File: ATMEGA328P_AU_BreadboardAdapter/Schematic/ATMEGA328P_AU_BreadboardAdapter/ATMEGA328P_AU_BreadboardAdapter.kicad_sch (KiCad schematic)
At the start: 23 parts, among them J1 FTDI, J2 Pin header 1, J3 Pin header 2, SW1 RESET, U1 AMS1117-5.0, U2 ATMEGA328P-AU, Y1 16MHz

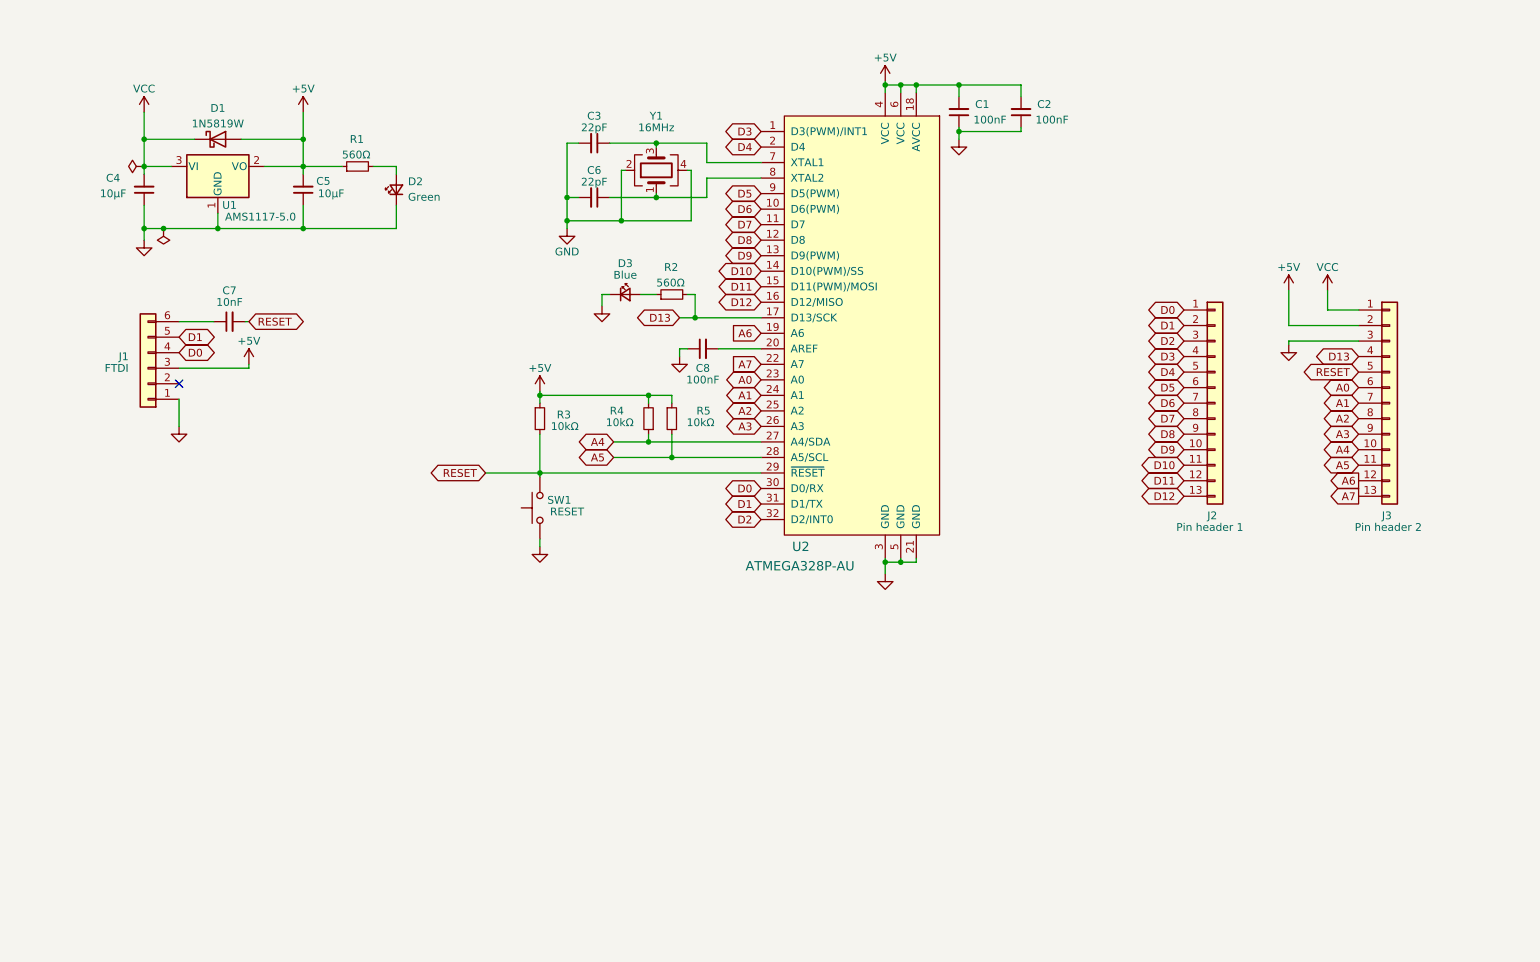
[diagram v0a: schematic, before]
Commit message: LDO replaced by buck regulator
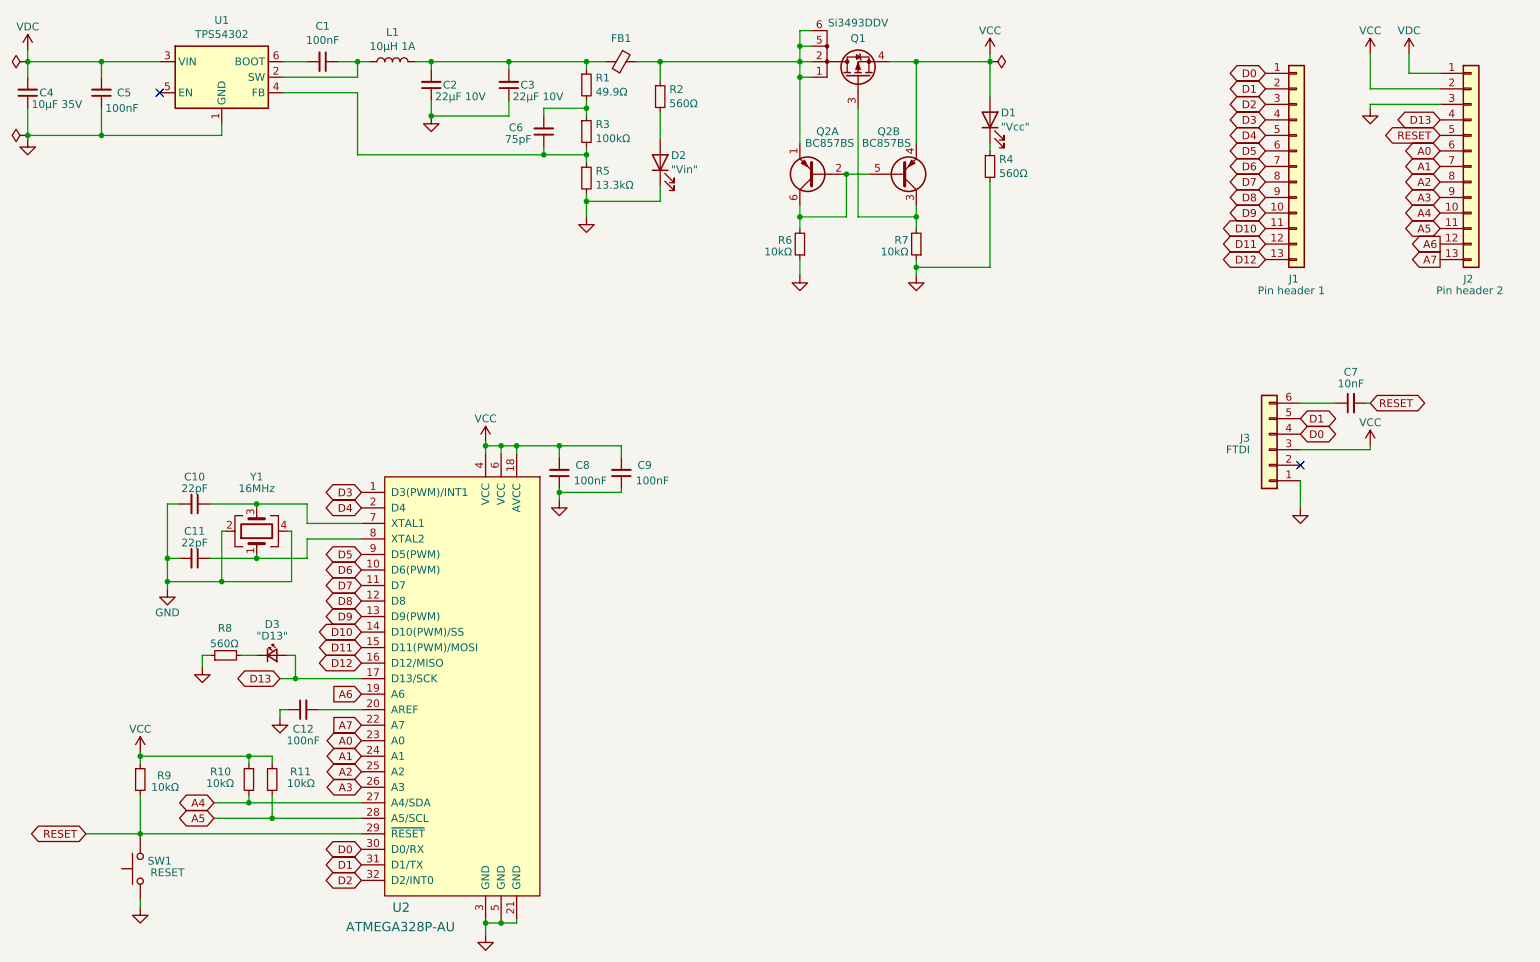
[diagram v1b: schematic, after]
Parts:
- removed D1: 1N5819W, Diode_SMD:D_SOD-123F, symbol Device:D_Schottky
- removed D2: Green, LED_SMD:LED_0603_1608Metric_Pad1.05x0.95mm_HandSolder, symbol Device:LED_Small
- removed U1: AMS1117-5.0, Package_TO_SOT_SMD:SOT-223-3_TabPin2, symbol Regulator_Linear:AMS1117-5.0
- added C1: 100nF, Capacitor_SMD:C_0603_1608Metric_Pad1.08x0.95mm_HandSolder, symbol Device:C_Small
- added C2, C3: 22µF 10V, Capacitor_SMD:C_0603_1608Metric_Pad1.08x0.95mm_HandSolder, symbol Device:C_Small
- added C6: 75pF, Capacitor_SMD:C_0603_1608Metric_Pad1.08x0.95mm_HandSolder, symbol Device:C_Small
- added D1: "Vcc", LED_SMD:LED_0603_1608Metric_Pad1.05x0.95mm_HandSolder, symbol Device:LED
- added D2: "Vin", LED_SMD:LED_0603_1608Metric_Pad1.05x0.95mm_HandSolder, symbol Device:LED
- added FB1: FerriteBead_Small, Inductor_SMD:L_0603_1608Metric_Pad1.05x0.95mm_HandSolder, symbol Device:FerriteBead_Small
- added L1: 10µH 1A, Inductor_SMD:L_Taiyo-Yuden_NR-20xx_HandSoldering, symbol Device:L
- added Q1: Si3493DDV, SamacSys_Parts:SOT95P280X100-6N, symbol myDevices:Si3493DDV
- added Q2: BC857BS, myDevices:SOT-363_SC-70-6-Handsoldering, symbol Transistor_BJT:BC857BS
- added R2, R4: 560Ω, Resistor_SMD:R_0603_1608Metric_Pad0.98x0.95mm_HandSolder, symbol Device:R_Small
- added R3: 100kΩ, Resistor_SMD:R_0603_1608Metric_Pad0.98x0.95mm_HandSolder, symbol Device:R_Small
- added R5: 13.3kΩ, Resistor_SMD:R_0603_1608Metric_Pad0.98x0.95mm_HandSolder, symbol Device:R_Small
- added R6, R7: 10kΩ, Resistor_SMD:R_0603_1608Metric_Pad0.98x0.95mm_HandSolder, symbol Device:R_Small
- added U1: TPS54302, Package_TO_SOT_SMD:SOT-23-6_Handsoldering, symbol Regulator_Switching:TPS54302
- C4: value 10µF -> 10µF 35V
- C5: value 10µF -> 100nF
- D3: value Blue -> "D13"
- R1: value 560Ω -> 49.9Ω
- renumbered C3 to C10, C6 to C11, C8 to C12, C1 to C8, C2 to C9, J2 to J1, J3 to J2, J1 to J3, R4 to R10, R5 to R11, R2 to R8, R3 to R9
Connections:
- net D13: now also D3.2 (A); no longer R8.2
- net GND: now also R8.1, C2.1, C3.1, D2.1 (K), R4.2, R5.2, R6.1, R7.1, U1.1 (GND); no longer D3.1 (K)
- net VCC: now also C8.2, C9.2, J2.2 (Pin_2), J3.3 (Pin_3), R10.2, R11.1, R9.1, U2.18 (AVCC), U2.4 (VCC), U2.6 (VCC), D1.2 (A), Q1.4 (S), Q2.4 (E2); no longer C4.2, J2.1 (Pin_1)
- net at R1.2: now also C6.2, R3.1
- removed net +5V: C5.2, C8.2, C9.2, J2.2 (Pin_2), J3.3 (Pin_3), R1.1, R10.2, R11.1, R9.1, U2.18 (AVCC), U2.4 (VCC), U2.6 (VCC)
- new net: C2.2, C3.2, FB1.1, L1.2, R1.1
- new net: D1.1 (K), R4.1
- new net: D3.1 (K), R8.2
- new net: Q2.2 (B1), Q2.5 (B2), Q2.6 (C1), R6.2
- new net: C6.1, R3.2, R5.1, U1.4 (FB)
- new net: D2.2 (A), R2.2
- new net: C1.1, L1.1, U1.2 (SW)
- new net: C1.2, U1.6 (BOOT)
- new net: FB1.2, Q1.1 (D), Q1.2 (D), Q1.5 (D), Q1.6 (D), Q2.1 (E1), R2.1
- new net: Q1.3 (G), Q2.3 (C2), R7.2
- new net VDC: C4.2, C5.2, J2.1 (Pin_1), U1.3 (VIN)
- no-connect marks 1 -> 2
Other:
- moved on the sheet: C10, C11, C12, C7, C8, C9, D3, J1, J2, J3, R10, R11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
